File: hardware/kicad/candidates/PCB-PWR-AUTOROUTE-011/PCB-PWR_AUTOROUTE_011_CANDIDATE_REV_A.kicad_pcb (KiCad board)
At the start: 4 copper layers, 90 x 60 mm, 66 parts, among them J1 43045-0213, J2 43045-1202, Q1 CSD18540Q5B, U1 LM74700QDBVRQ1, U2 INA226AIDGSR, U3 LMR604403SRAKR, U4 LMR604403SRAKR, U5 TPS7A2018PDBVR

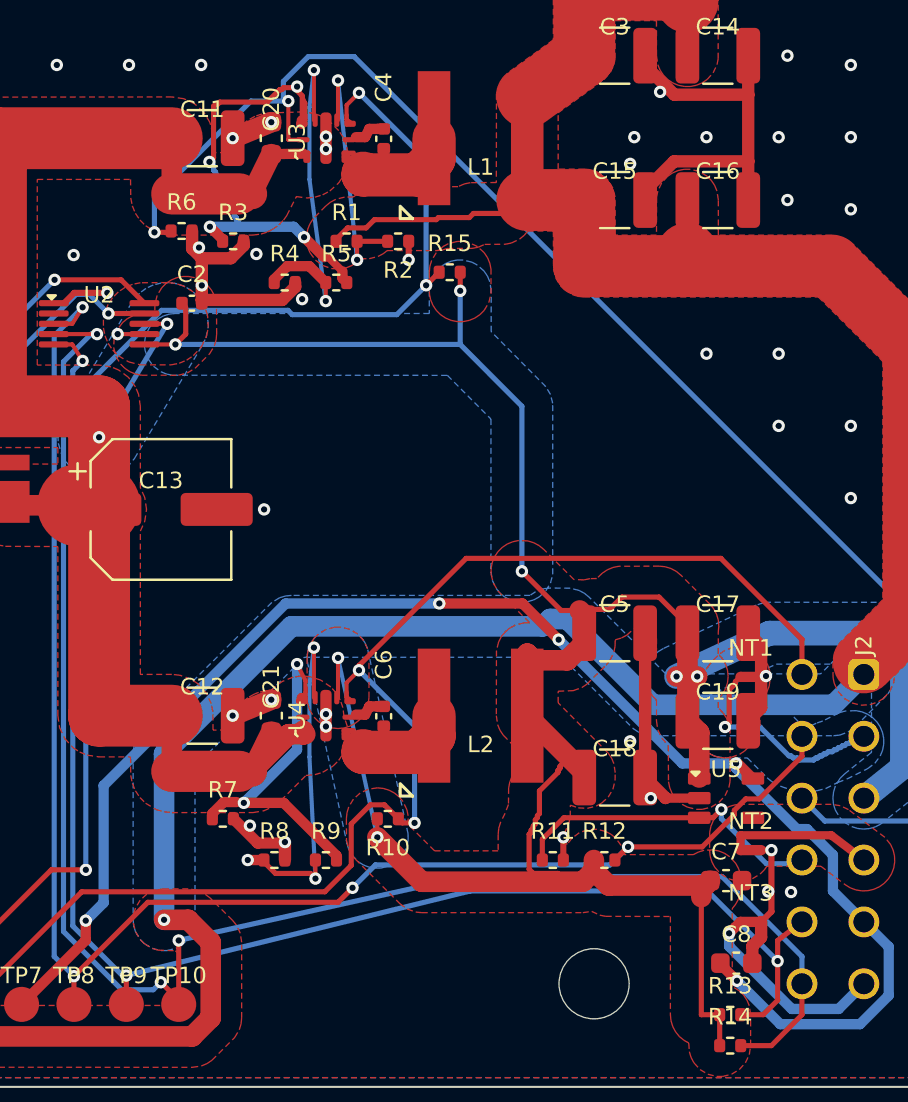
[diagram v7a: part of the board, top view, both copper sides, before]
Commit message: apply: tools/apply_pcb_pwr_autoroute_candidate_rev_a.py
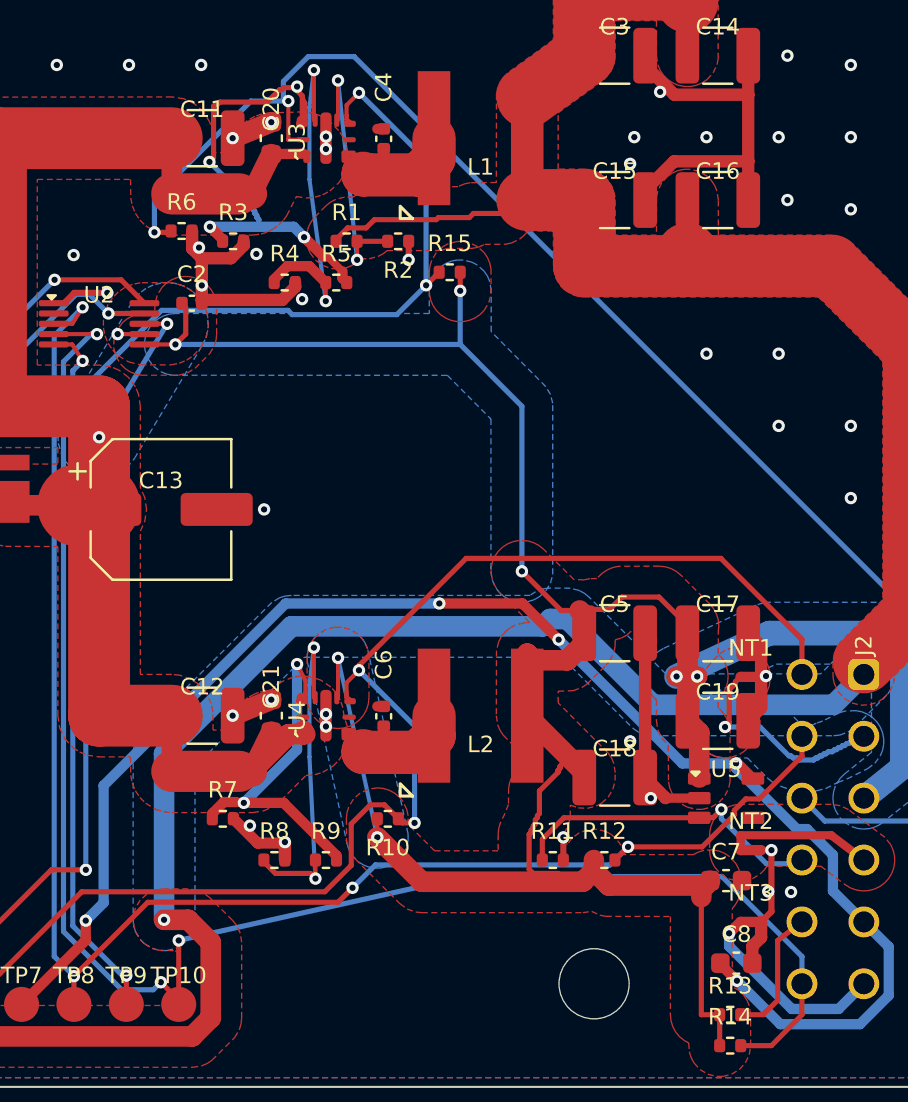
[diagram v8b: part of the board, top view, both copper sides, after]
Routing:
- net I2C2_SCL: track 74.4 -> 40.9 mm, vias 3 -> 2
- net BOOT_3V3: track 1.60 -> 0.31 mm
- net BOOT_3V8: track 1.60 -> 0.31 mm
- net MODE_3V3: track 18.0 -> 17.2 mm, vias 3 -> 2
